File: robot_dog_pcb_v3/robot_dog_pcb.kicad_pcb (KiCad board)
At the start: 2 copper layers, 4 parts, among them J3 Conn_01x04_Socket, U1 ESP32-C3_SUPERMINI_TH, U2 Adafruit-MAX98357-I2S-Amp-Bre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, U3 Adafruit-16-Channel-PWM-Servo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

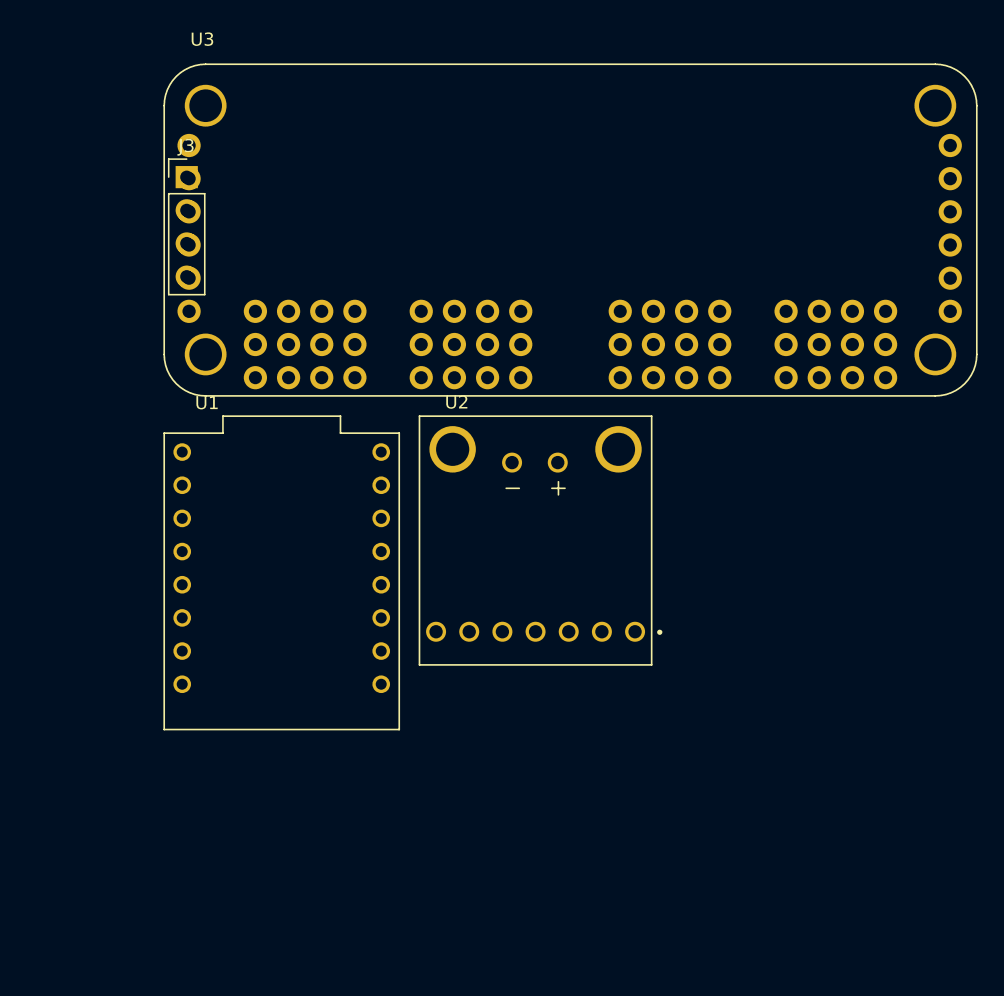
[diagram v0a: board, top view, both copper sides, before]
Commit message: design with pin placement, extra pins and traces done
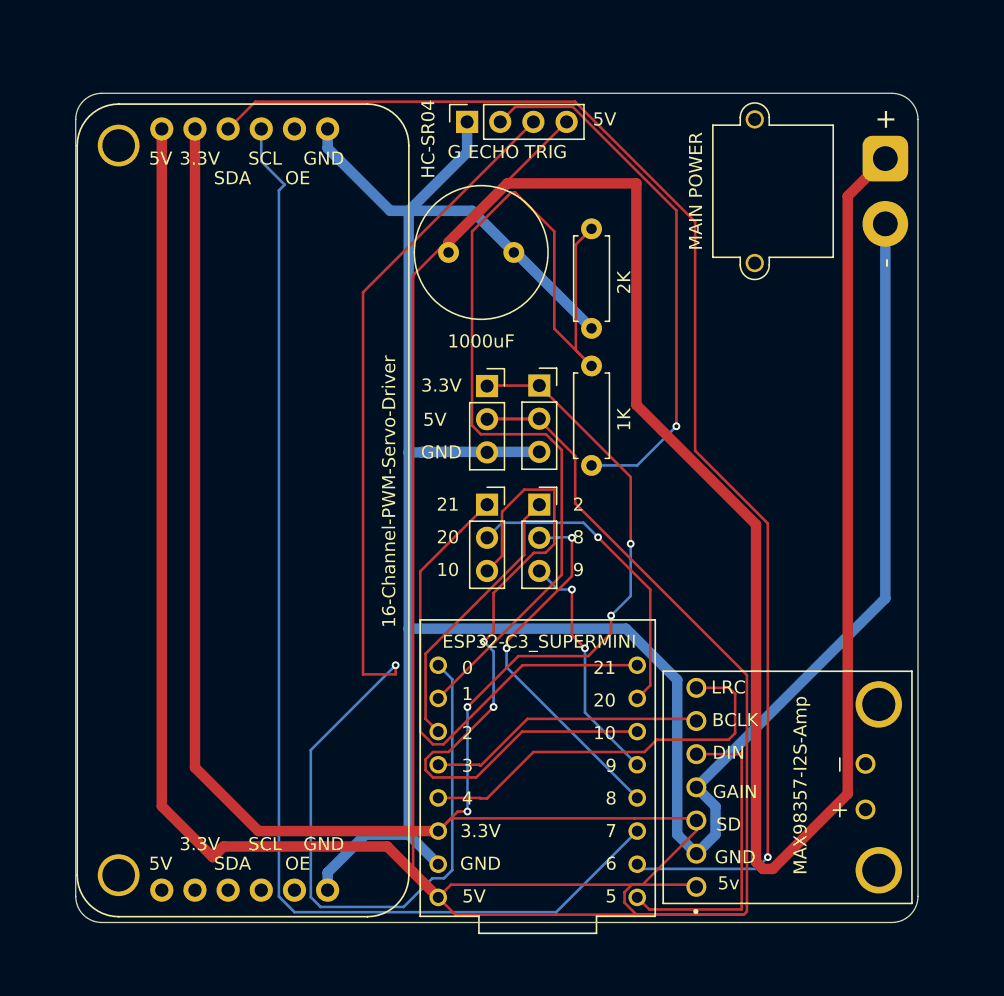
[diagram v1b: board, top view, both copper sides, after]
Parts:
- removed J3: Conn_01x04_Socket, Connector_PinHeader_2.54mm:PinHeader_1x04_P2.54mm_Vertical
- removed U2: Adafruit-MAX98357-I2S-Amp-Breakout, robot_Library:Adafruit-MAX98357-I2S-Amp-Breakout
- added 1000uF: 1000uF, Capacitor_THT:C_Radial_D10.0mm_H12.5mm_P5.00mm, F.Cu at (91.0, 74.2)
- added 1K: 1k, Resistor_THT:R_Axial_DIN0207_L6.3mm_D2.5mm_P7.62mm_Horizontal, F.Cu at (102.0, 90.5)
- added 2K: 2K, Resistor_THT:R_Axial_DIN0207_L6.3mm_D2.5mm_P7.62mm_Horizontal, F.Cu at (102.0, 80.0)
- added 5V: Extra power, Connector_PinSocket_2.54mm:PinSocket_1x03_P2.54mm_Vertical, F.Cu at (94.0, 84.4)
- added GPIO: GPIO, Connector_PinSocket_2.54mm:PinSocket_1x03_P2.54mm_Vertical, F.Cu at (94.0, 93.5)
- added HC-SR04 : HC-SR04 sensor, Connector_PinSocket_2.54mm:PinSocket_1x04_P2.54mm_Vertical, F.Cu at (92.5, 64.2)
- added J4: GPIO, Connector_PinSocket_2.54mm:PinSocket_1x03_P2.54mm_Vertical, F.Cu at (98.0, 93.5)
- added J6: Extra power, Connector_PinSocket_2.54mm:PinSocket_1x03_P2.54mm_Vertical, F.Cu at (98.0, 84.4)
- added MAIN POWER: , Connector_AMASS:AMASS_XT30PW-M_1x02_P2.50mm_Horizontal, F.Cu at (124.5, 67.0)
- added MAX98357-I2S-Amp: Adafruit-MAX98357-I2S-Amp-Breakout, robot_Library:Adafruit-MAX98357-I2S-Amp-Breakout, F.Cu at (117.0, 115.2)
- 16-Channel-PWM-Servo-Driver: renamed from U3; value Adafruit-16-Channel-PWM-Servo-Driver-PCB -> PCB ONLY Adafruit-16-Channel-PWM-Servo-Driver-PCB; footprint robot_Library:Adafruit-16-Channel-PWM-Servo-Driver-PCB -> robot_Library:PCB ONLY Adafruit-16-Channel-PWM-Servo-Driver-PCB
- ESP32-C3_SUPERMINI: renamed from U1; value ESP32-C3_SUPERMINI_TH -> ESP32-C3_SUPERMINI
- moved 16-Channel-PWM-Servo-Driver 33.0 mm to (75.3, 93.9), turned to -90 degrees
- moved ESP32-C3_SUPERMINI 24.3 mm to (97.9, 113.7), turned to 180 degrees
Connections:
- 16-Channel-PWM-Servo-Driver pad OE_1: Net-(U3-~{OE}-PadOE_1) -> unconnected-(U3-~{OE}-PadOE_1)_1
- 16-Channel-PWM-Servo-Driver pad OE_2: Net-(U3-~{OE}-PadOE_1) -> unconnected-(U3-~{OE}-PadOE_1)
- 16-Channel-PWM-Servo-Driver pad SCL_1: /SDA -> Net-(U1-GPIO7)
- 16-Channel-PWM-Servo-Driver pad SCL_2: /SDA -> Net-(U1-GPIO7)
- 16-Channel-PWM-Servo-Driver pad SDA_1: /SCL -> Net-(U1-GPIO6)
- 16-Channel-PWM-Servo-Driver pad SDA_2: /SCL -> Net-(U1-GPIO6)
- 16-Channel-PWM-Servo-Driver pad V+_1: V+ -> +5V screw terminal
- 16-Channel-PWM-Servo-Driver pad V+_2: V+ -> +5V screw terminal
- 16-Channel-PWM-Servo-Driver pad VCC_1: VCC -> +5V screw terminal
- 16-Channel-PWM-Servo-Driver pad VCC_2: VCC -> +5V screw terminal
- ESP32-C3_SUPERMINI pad 1: /ECHO_DIV -> Net-(U1-GPIO1)
- ESP32-C3_SUPERMINI pad 10: unconnected-(U1-GPIO10-Pad10) -> Net-(J2-Pin_3)
- ESP32-C3_SUPERMINI pad 2: unconnected-(U1-GPIO2-Pad2) -> Net-(J4-Pin_1)
- ESP32-C3_SUPERMINI pad 20: unconnected-(U1-GPIO20-Pad20) -> Net-(J2-Pin_2)
- ESP32-C3_SUPERMINI pad 21: unconnected-(U1-GPIO21-Pad21) -> Net-(J2-Pin_1)
- ESP32-C3_SUPERMINI pad 3: /I2S_BCLK -> Net-(U1-GPIO3)
- ESP32-C3_SUPERMINI pad 3.3: Net-(U1-3V3) -> +5V screw terminal
- ESP32-C3_SUPERMINI pad 4: /I2S_LRCLK -> Net-(U1-GPIO4)
- ESP32-C3_SUPERMINI pad 5: /I2S_DOUT -> Net-(U1-GPIO5)
- ESP32-C3_SUPERMINI pad 5V: +5V -> +5V screw terminal
- ESP32-C3_SUPERMINI pad 6: unconnected-(U1-GPIO6-Pad6) -> Net-(U1-GPIO6)
- ESP32-C3_SUPERMINI pad 7: unconnected-(U1-GPIO7-Pad7) -> Net-(U1-GPIO7)
- ESP32-C3_SUPERMINI pad 8: /SDA -> Net-(J4-Pin_2)
- ESP32-C3_SUPERMINI pad 9: /SCL -> Net-(J4-Pin_3)
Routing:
- net +5V screw terminal: track 0.00 -> 527.1 mm, vias 0 -> 4
- net GND: track 0.00 -> 197.6 mm
- net Net-(U1-GPIO6): track 0.00 -> 101.9 mm, vias 0 -> 1
- net /TRIG: track 0.00 -> 99.8 mm, vias 0 -> 1
- net Net-(U1-GPIO7): track 0.00 -> 90.2 mm
- net Net-(U1-GPIO1): track 0.00 -> 77.2 mm
- net Net-(J2-Pin_3): track 0.00 -> 55.0 mm, vias 0 -> 2
- net /ECHO: track 0.00 -> 41.5 mm, vias 0 -> 1
- net Net-(J2-Pin_1): track 0.00 -> 39.3 mm
- net Net-(U1-GPIO4): track 0.00 -> 31.0 mm
- net Net-(J4-Pin_2): track 0.00 -> 28.7 mm, vias 0 -> 2
- net Net-(U1-GPIO5): track 0.00 -> 23.9 mm
- net Net-(J2-Pin_2): track 0.00 -> 23.8 mm, vias 0 -> 1
- net Net-(J4-Pin_1): track 0.00 -> 21.4 mm
- net Net-(U1-GPIO3): track 0.00 -> 21.4 mm
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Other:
- board outline added: 64.5 x 63.5 mm
- board text added: "0"
- board text added: "1"
- board text added: "10"
- board text added: "2"
- board text added: "20"
- board text added: "21"
- board text added: "3"
- board text added: "3.3V"
- board text added: "4"
- board text added: "5"
- board text added: "5V"
- board text added: "5v"
- board text added: "6"
- board text added: "7"
- board text added: "8"
- board text added: "9"
- board text added: "BCLK"
- board text added: "DIN"
- board text added: "ECHO"
- board text added: "G"
- board text added: "GAIN"
- board text added: "GND"
- board text added: "LRC"
- board text added: "OE"
- board text added: "SCL"
- board text added: "SD"
- board text added: "SDA"
- board text added: "TRIG"
- board text added: "need to measure the sensor pins"

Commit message: corrected pcb flags and wiring
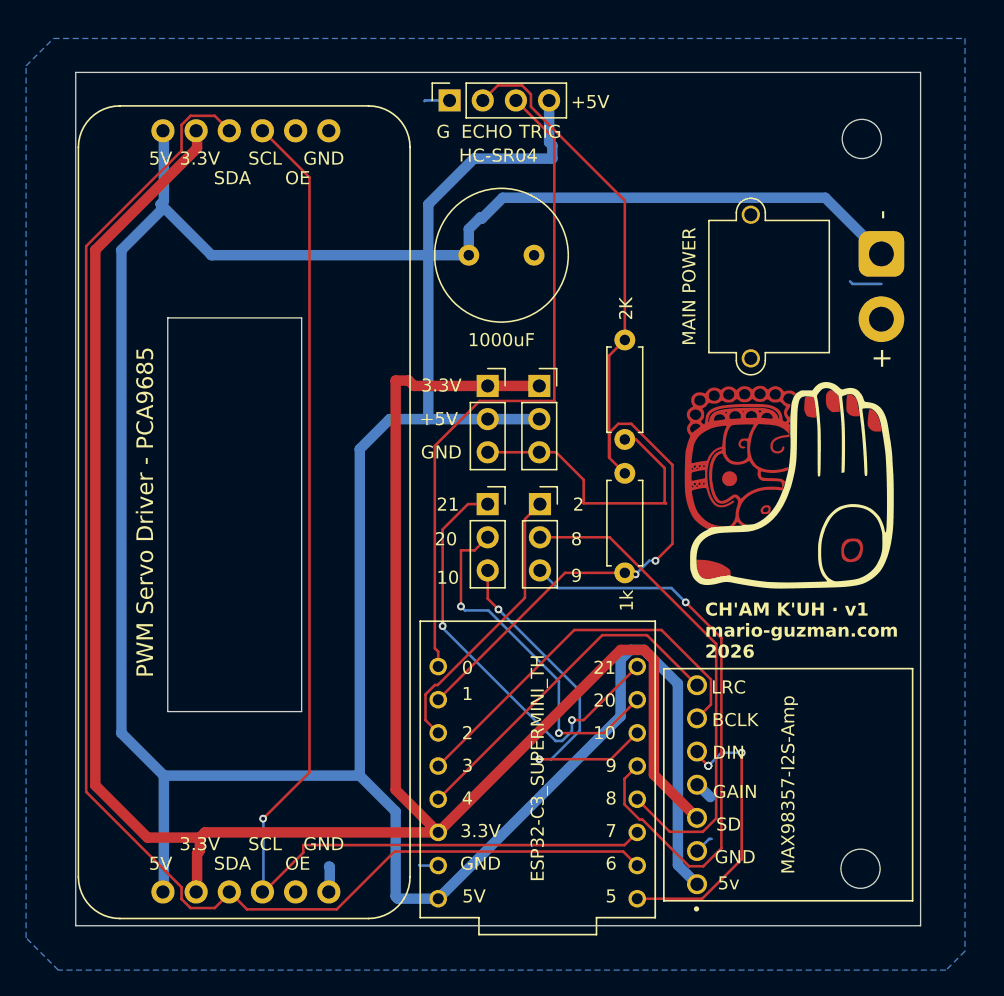
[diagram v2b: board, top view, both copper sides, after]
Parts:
- removed 1000uF: 1000uF, Capacitor_THT:C_Radial_D10.0mm_H12.5mm_P5.00mm
- removed 16-Channel-PWM-Servo-Driver: PCB ONLY Adafruit-16-Channel-PWM-Servo-Driver-PCB, robot_Library:PCB ONLY Adafruit-16-Channel-PWM-Servo-Driver-PCB
- removed 1K: 1k, Resistor_THT:R_Axial_DIN0207_L6.3mm_D2.5mm_P7.62mm_Horizontal
- removed 2K: 2K, Resistor_THT:R_Axial_DIN0207_L6.3mm_D2.5mm_P7.62mm_Horizontal
- removed 5V: Extra power, Connector_PinSocket_2.54mm:PinSocket_1x03_P2.54mm_Vertical
- removed ESP32-C3_SUPERMINI: ESP32-C3_SUPERMINI, robot_Library:MODULE_ESP32-C3_SUPERMINI_TH
- removed GPIO: GPIO, Connector_PinSocket_2.54mm:PinSocket_1x03_P2.54mm_Vertical
- removed HC-SR04 : HC-SR04 sensor, Connector_PinSocket_2.54mm:PinSocket_1x04_P2.54mm_Vertical
- removed MAIN POWER: , Connector_AMASS:AMASS_XT30PW-M_1x02_P2.50mm_Horizontal
- removed MAX98357-I2S-Amp: Adafruit-MAX98357-I2S-Amp-Breakout, robot_Library:Adafruit-MAX98357-I2S-Amp-Breakout
- added C1: 1000uF, Capacitor_THT:C_Radial_D10.0mm_H12.5mm_P5.00mm, F.Cu at (92.6, 74.4)
- added G***: LOGO, robot_Library:sello_unas_Cu, F.Cu at (116.7, 91.9)
- added G***: LOGO, robot_Library:sello_unas_Mask, F.Cu at (116.7, 91.9)
- added G***: LOGO, robot_Library:mano_Silk, F.Cu at (122.3, 92.0)
- added G***: LOGO, robot_Library:B_neg_mayan_robot_Silk, B.Cu at (97.2, 94.2)
- added H1: MountingHole, MountingHole:MountingHole_3mm, F.Cu at (122.6, 121.4)
- added H3: MountingHole, MountingHole:MountingHole_3mm, F.Cu at (122.7, 65.5)
- added J1: MAIN POWER, Connector_AMASS:AMASS_XT30PW-M_1x02_P2.50mm_Horizontal, F.Cu at (124.2, 74.3)
- added J2: GPIO, Connector_PinSocket_2.54mm:PinSocket_1x03_P2.54mm_Vertical, F.Cu at (94.0, 93.5)
- added J3: HC-SR04, Connector_PinSocket_2.54mm:PinSocket_1x04_P2.54mm_Vertical, F.Cu at (91.1, 62.5)
- added J5: Extra power, Connector_PinSocket_2.54mm:PinSocket_1x03_P2.54mm_Vertical, F.Cu at (94.0, 84.4)
- added R2: 2K, Resistor_THT:R_Axial_DIN0207_L6.3mm_D2.5mm_P7.62mm_Horizontal, F.Cu at (104.5, 88.5)
- added R3: 1k, Resistor_THT:R_Axial_DIN0207_L6.3mm_D2.5mm_P7.62mm_Horizontal, F.Cu at (104.5, 98.7)
- added U1: ESP32-C3_SUPERMINI_TH, robot_Library:MODULE_ESP32-C3_SUPERMINI_TH, F.Cu at (97.9, 113.8)
- added U2: MAX98357-I2S-Amp, robot_Library:Adafruit-MAX98357-I2S-Amp-Breakout, F.Cu at (117.1, 115.0)
- added U3: Adafruit-16-Channel-PWM-Servo-Driver-PCB, robot_Library:PCB ONLY Adafruit-16-Channel-PWM-Servo-Driver-PCB, F.Cu at (75.4, 94.1)
- moved J4 0.06 mm to (98.0, 93.5)
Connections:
- J4 pad 1: Net-(J4-Pin_1) -> /GPI02
- J4 pad 2: Net-(J4-Pin_2) -> /GPI08
- J4 pad 3: Net-(J4-Pin_3) -> /GPI09
- J6 pad 1: +5V screw terminal -> VCC
- J6 pad 2: +5V screw terminal -> V+
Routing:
- net +5V screw terminal: track 527.1 -> 0.00 mm, vias 4 -> 0
- net V+: track 0.00 -> 268.7 mm
- net VCC: track 0.00 -> 168.9 mm
- net GND: track 197.6 -> 36.1 mm
- net /SDA: track 0.00 -> 108.3 mm
- net Net-(U1-GPIO6): track 101.9 -> 0.00 mm, vias 1 -> 0
- net /SCL: track 0.00 -> 92.2 mm, vias 0 -> 1
- net Net-(U1-GPIO7): track 90.2 -> 0.00 mm
- net Net-(U1-GPIO1): track 77.2 -> 0.00 mm
- net Net-(J2-Pin_3): track 55.0 -> 0.00 mm, vias 2 -> 0
- net /TRIG: track 99.8 -> 52.2 mm, vias 1 -> 0
- net /GPI09: track 0.00 -> 45.4 mm, vias 0 -> 1
- net Net-(J2-Pin_1): track 39.3 -> 0.00 mm
- net /GPI08: track 0.00 -> 37.7 mm
- net /ECHO: track 41.5 -> 74.8 mm, vias 1 -> 2
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- added copper zone on B.Cu, net GND
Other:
- board size 64.5 x 63.5 mm -> 64.7 x 65.3 mm
- board text added: "+5V"
- board text added: "CH'AM K'UH · v1 mario-guzman.com 2026"
- board text removed: "need to measure the sensor pins"
